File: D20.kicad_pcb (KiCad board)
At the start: 6 copper layers, 14 x 7.9 mm, 49 parts, among them IC1 AVR64DD28-I_STX, IC2 NCP730BM, IC3 DRV8231ADSGR, J1 NEM651, J10 Conn_01x01, J2 Conn_01x01, J3 NEM651, J4 Conn_01x01, J5 Conn_01x01, J6 Conn_01x01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

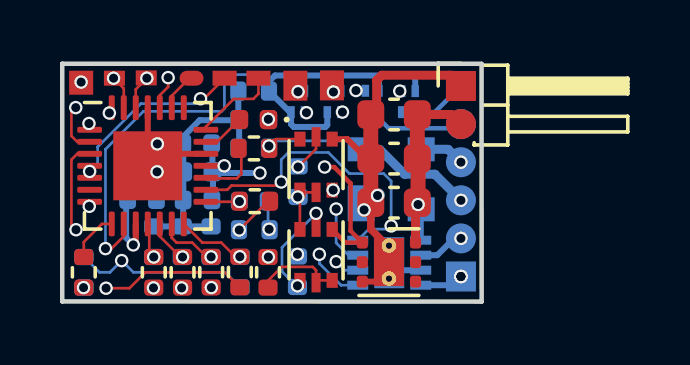
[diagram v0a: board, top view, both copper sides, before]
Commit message: add: clamping diode
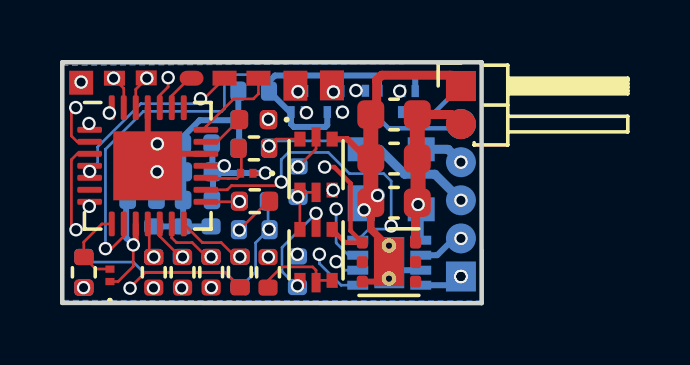
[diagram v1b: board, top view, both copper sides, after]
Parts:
- added D3: BAT30F4, RTB:BAT30F4, F.Cu at (59.6, -45.0)
- added D4: BAT30F4, RTB:BAT30F4, F.Cu at (55.1, -41.6)
- R1, R2: value 100k -> 68k
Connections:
- net Net-(IC1-Pad17) renamed DCC-b'
- net Net-(IC1-Pad8) renamed DCC-a'
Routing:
- net +3V3: track 15.5 -> 17.8 mm
- net GND: track 37.7 -> 39.5 mm, vias 7 -> 6
- net DCC-b: track 28.6 -> 27.0 mm
- net DCC-a': track 1.68 -> 2.71 mm
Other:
- board size 14 x 7.9 mm -> 14 x 8 mm
- board text added: "fs24 D20.1"
- board text removed: "fs24 D20.0"

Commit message: add: fuses
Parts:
- C1: value 22u -> 22u/4V
- C2: value 22u/25V -> 10u/25V
- J2, J9: value Conn_01x01 -> pad
- J3: value NEM651 -> Capacitor
- R1, R2: value 68k -> 33k
- R13: value 3.3k -> 1k
- R16, R18: value 10k -> 12k

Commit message: updated Kicad version
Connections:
- IC1 pad 22: (no net) -> unconnected-(IC1-PF6_(~{RESET})-Pad22)
- IC1 pad 6: (no net) -> unconnected-(IC1-PC0-Pad6)
- IC2 pad 2: (no net) -> unconnected-(IC2-NC/ADJ-Pad2)
- IC2 pad 4: (no net) -> unconnected-(IC2-EN-Pad4)
- IC2 pad 5: (no net) -> unconnected-(IC2-NC/PG-Pad5)
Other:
- net class Default removed
- net class Power removed
